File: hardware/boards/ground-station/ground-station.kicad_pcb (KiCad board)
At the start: 4 copper layers, 65 x 59.5 mm, 122 parts, among them J1 USB_A, J101 Raspberry_Pi_2_3, J102 Conn_01x15, J2 Barrel_Jack, J201 U.FL, J202 U.FL, J203 U.FL, J3 Conn_Coaxial, U201 SX1262IMLTRT, U202 RX5808, U203 SW-GPS01, U204 SKY13453-385LF, U3 TPS564242DRLR, U601 ADV7282A-M, U602 AP2127K-1.8, U603 AP2127K-1.8, Y201 32 MHz, Y601 28.63636 MHz

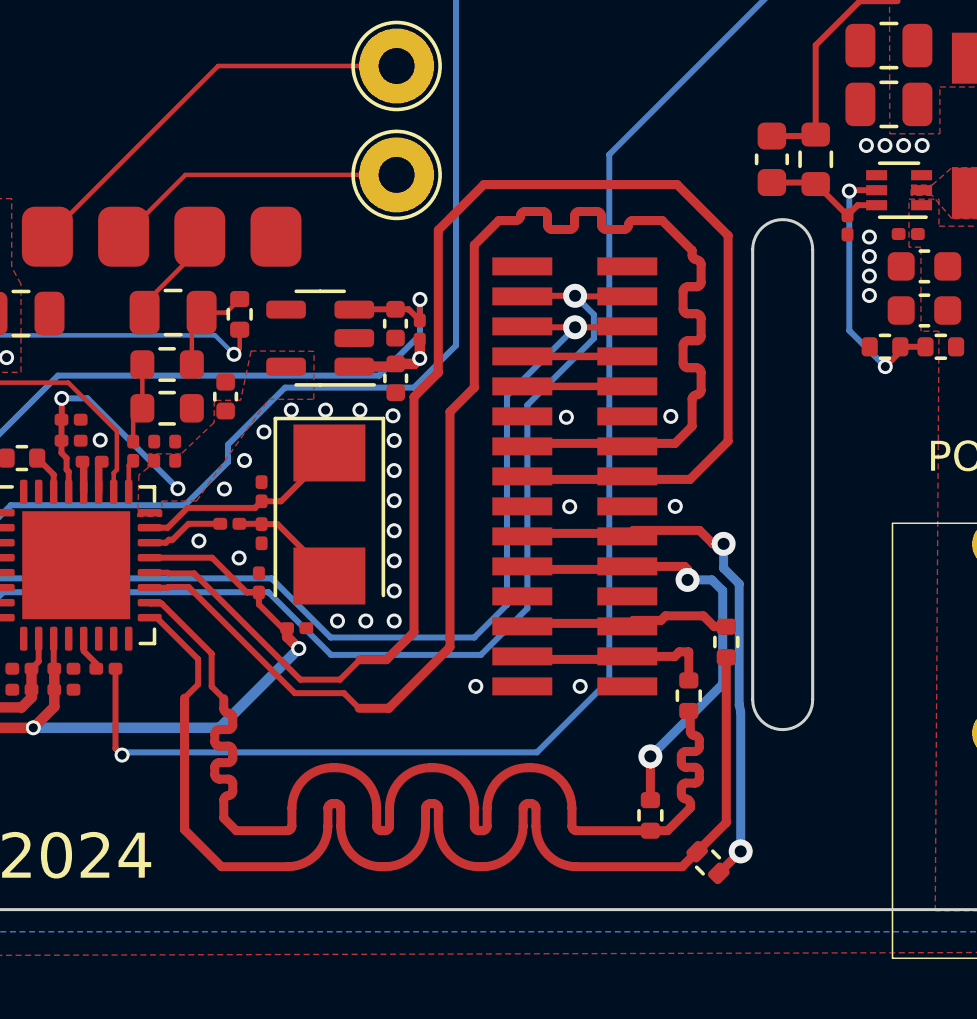
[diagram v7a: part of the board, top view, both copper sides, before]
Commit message: pair length match fix
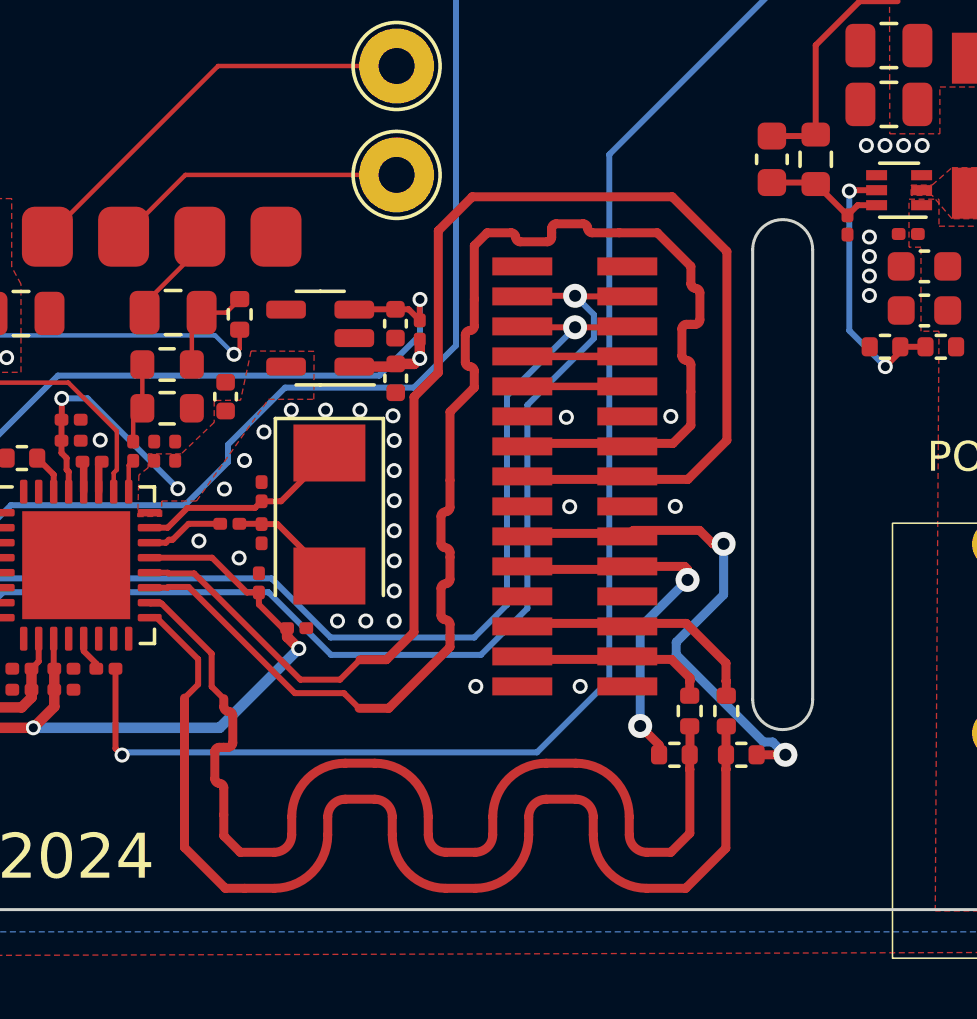
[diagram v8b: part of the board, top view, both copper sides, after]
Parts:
- moved R24 3.76 mm to (143.8, 120.2), turned to 0 degrees
- moved R26 2.30 mm to (143.3, 118.8)
- moved R23 2.17 mm to (141.6, 120.2), turned to 180 degrees
- moved R25 0.51 mm to (142.1, 118.8)
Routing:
- net +5V: track 54.0 -> 50.8 mm
- net /CAM_D0_N: track 39.9 -> 36.8 mm
- net /CAM_D1_CONN_N: track 15.3 -> 12.7 mm
- net /CAM_CK_P: track 50.1 -> 47.9 mm
- net /CAM_D0_P: track 41.1 -> 39.3 mm
- net /CAM_D0_CONN_P: track 7.18 -> 8.55 mm
- net /CAM_D1_CONN_P: track 18.6 -> 17.4 mm
- net /CAM_CK_N: track 50.0 -> 49.3 mm
